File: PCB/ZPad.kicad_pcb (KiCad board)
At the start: 2 copper layers, 82 x 65.2 mm, 19 parts, among them J1 Conn_01x04, SW1 SW_Push, SW2 SW_Push, SW3 SW_Push, SW4 SW_Push, SW5 SW_Push, SW6 SW_Push, SW7 SW_Push, SW8 SW_Push, SW9 RotaryEncoder_Switch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

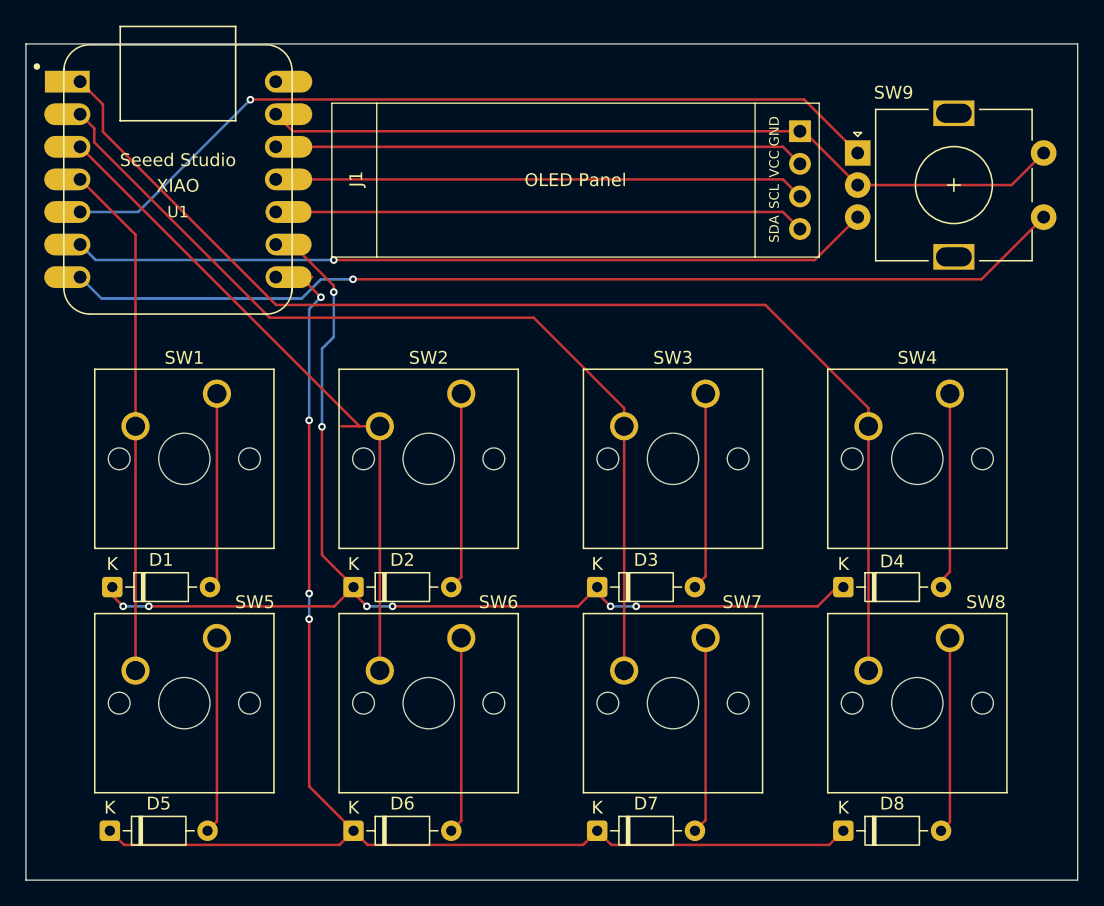
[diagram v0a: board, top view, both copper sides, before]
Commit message: Fixed stuff according to reviewer
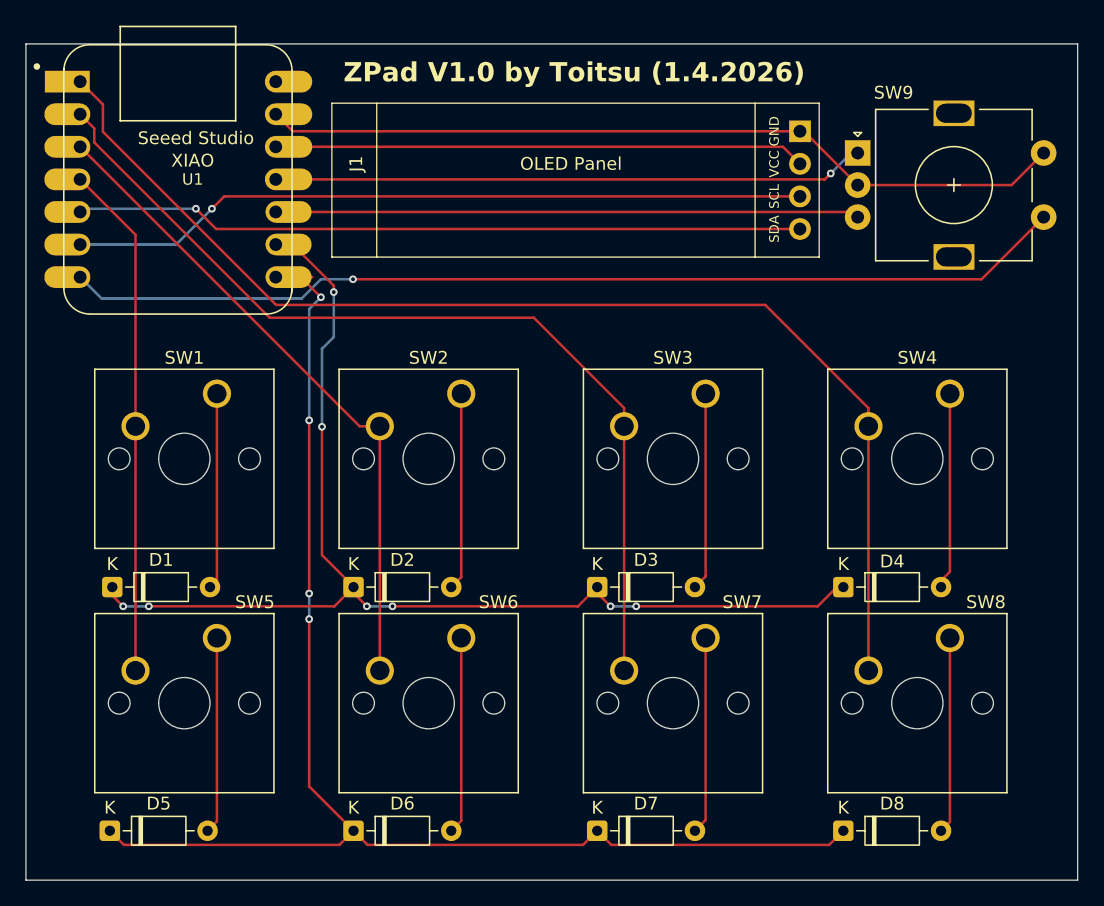
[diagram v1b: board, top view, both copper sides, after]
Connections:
- U1 pad 10: /SDA -> /Rotary_Sw_B
- U1 pad 11: /SCL -> /Rotary_Sw_A
- U1 pad 5: /Rotary_Sw_A -> /SDA
- U1 pad 6: /Rotary_Sw_B -> /SCL
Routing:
- net /Rotary_Sw_A: track 66.0 -> 47.3 mm
- net /Rotary_Sw_B: track 62.5 -> 45.5 mm, vias 1 -> 0
- net /SDA: track 41.4 -> 56.9 mm, vias 0 -> 1
- net /SCL: track 42.5 -> 57.7 mm, vias 0 -> 1
- net /COL1: track 52.9 -> 51.4 mm
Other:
- board text added: "ZPad V1.0 by Toitsu (1.4.2026)"
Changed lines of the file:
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@@
 		(at 128.35 64.27)
 		(property "Reference" "J1"
-			(at 1.9 5.91 90)
+			(at 1.9 4.73 90)
 			(layer "F.SilkS")
 			(effects
@@
 		)
 		(property "Value" "Conn_01x04"
-			(at 18.5 14 0)
+			(at 18.15 12.98 0)
 			(layer "F.Fab")
 			(effects
@@
 		)
 		(fp_text user "OLED Panel"
-			(at 19 6 0)
+			(at 18.65 4.73 0)
 			(layer "F.SilkS")
 			(effects
@@
 		)
 		(property "Value" "RotaryEncoder_Switch"
-			(at 7.5 10.4 0)
+			(at 7.5 10.845 0)
 			(layer "F.Fab")
 			(effects
@@
 		(at 116.35 70.212015)
 		(property "Reference" "U1"
-			(at 0 2.54 0)
+			(at 1.15 0 0)
 			(layer "F.SilkS")
 			(effects
@@
 		)
 		(fp_text user "Seeed Studio"
-			(at 0 -1.5 0)
+			(at 1.4 -3.212015 0)
 			(unlocked yes)
 			(layer "F.SilkS")
@@
 		)
 		(fp_text user "XIAO"
-			(at 0 0.5 0)
+			(at 1.15 -1.462015 0)
 			(unlocked yes)
 			(layer "F.SilkS")
@@
 			(layers "*.Cu" "*.Mask")
 			(remove_unused_layers no)
-			(net 21 "/Rotary_Sw_A")
+			(net 12 "/SDA")
 			(pinfunction "PA8_A4_D4_SDA")
 			(pintype "passive")
@@
 			(layers "*.Cu" "*.Mask")
 			(remove_unused_layers no)
-			(net 20 "/Rotary_Sw_B")
+			(net 13 "/SCL")
 			(pinfunction "PA9_A5_D5_SCL")
 			(pintype "passive")
@@
 			(layers "*.Cu" "*.Mask")
 			(remove_unused_layers no)
-			(net 12 "/SDA")
+			(net 20 "/Rotary_Sw_B")
 			(pinfunction "PA5_A9_D9_MISO")
 			(pintype "passive")
@@
 			(layers "*.Cu" "*.Mask")
 			(remove_unused_layers no)
-			(net 13 "/SCL")
+			(net 21 "/Rotary_Sw_A")
 			(pinfunction "PA6_A10_D10_MOSI")
 			(pintype "passive")
@@
 		(layer "Edge.Cuts")
 	)
+	(gr_text "ZPad V1.0 by Toitsu (1.4.2026)"
+		(at 129.25 62.75 0)
+		(layer "F.SilkS")
+		(effects
+			(font
+				(size 1.5 1.5)
+				(thickness 0.3)
+				(bold yes)
+			)
+			(justify left bottom)
+		)
+	)
 	(segment
 		(start 128.5 78.5)
@@
 	(segment
 		(start 164.85 74.08)
-		(end 163.522015 72.752015)
+		(end 119.33 74.08)
 		(width 0.2)
 		(layer "F.Cu")
@@
 	)
 	(segment
-		(start 163.522015 72.752015)
-		(end 123.975 72.752015)
+		(start 119.33 74.08)
+		(end 117.75 72.5)
 		(width 0.2)
 		(layer "F.Cu")
 		(net 12)
 	)
+	(via
+		(at 117.75 72.5)
+		(size 0.6)
+		(drill 0.3)
+		(layers "F.Cu" "B.Cu")
+		(net 12)
+	)
 	(segment
-		(start 163.522015 70.212015)
-		(end 123.975 70.212015)
+		(start 117.75 72.5)
+		(end 108.977015 72.5)
+		(width 0.2)
+		(layer "B.Cu")
+		(net 12)
+	)
+	(segment
+		(start 108.977015 72.5)
+		(end 108.725 72.752015)
+		(width 0.2)
+		(layer "B.Cu")
+		(net 12)
+	)
+	(segment
+		(start 164.85 71.54)
+		(end 119.96 71.54)
 		(width 0.2)
 		(layer "F.Cu")
@@
 	)
 	(segment
-		(start 164.85 71.54)
-		(end 163.522015 70.212015)
+		(start 119.96 71.54)
+		(end 119 72.5)
 		(width 0.2)
 		(layer "F.Cu")
 		(net 13)
 	)
+	(via
+		(at 119 72.5)
+		(size 0.6)
+		(drill 0.3)
+		(layers "F.Cu" "B.Cu")
+		(net 13)
+	)
 	(segment
-		(start 125.01276 70.212015)
-		(end 123.975 70.212015)
+		(start 119 72.5)
+		(end 116.207985 75.292015)
+		(width 0.2)
+		(layer "B.Cu")
+		(net 13)
+	)
+	(segment
+		(start 116.207985 75.292015)
+		(end 108.725 75.292015)
 		(width 0.2)
 		(layer "B.Cu")
@@
 	)
 	(segment
-		(start 132.09 89.46)
-		(end 129.092985 89.46)
+		(start 130.512985 89.46)
+		(end 132.09 89.46)
 		(width 0.2)
 		(layer "F.Cu")
@@
 	)
 	(segment
-		(start 166.005 76.5)
-		(end 128.5 76.5)
+		(start 168.947015 72.752015)
+		(end 169.35 73.155)
 		(width 0.2)
 		(layer "F.Cu")
@@
 	)
 	(segment
-		(start 169.35 73.155)
-		(end 166.005 76.5)
+		(start 123.975 72.752015)
+		(end 168.947015 72.752015)
 		(width 0.2)
 		(layer "F.Cu")
 		(net 20)
 	)
-	(via
-		(at 128.5 76.5)
-		(size 0.6)
-		(drill 0.3)
-		(layers "F.Cu" "B.Cu")
-		(net 20)
-	)
-	(segment
-		(start 109.932985 76.5)
-		(end 108.725 75.292015)
-		(width 0.2)
-		(layer "B.Cu")
-		(net 20)
-	)
-	(segment
-		(start 128.5 76.5)
-		(end 109.932985 76.5)
-		(width 0.2)
-		(layer "B.Cu")
-		(net 20)
-	)
 	(segment
-		(start 122.018985 63.981015)
-		(end 122 64)
+		(start 166.787985 70.212015)
+		(end 167.25 69.75)
 		(width 0.2)
 		(layer "F.Cu")
@@
 	)
 	(segment
-		(start 165.176015 63.981015)
-		(end 122.018985 63.981015)
-		(width 0.2)
-		(layer "F.Cu")
-		(net 21)
-	)
-	(segment
-		(start 169.35 68.155)
-		(end 165.176015 63.981015)
+		(start 123.975 70.212015)
+		(end 166.787985 70.212015)
 		(width 0.2)
 		(layer "F.Cu")
@@
 	)
 	(via
-		(at 122 64)
+		(at 167.25 69.75)
 		(size 0.6)
 		(drill 0.3)
@@
 	)
 	(segment
-		(start 122 64)
-		(end 113.247985 72.752015)
+		(start 168.845 68.155)
+		(end 169.35 68.155)
 		(width 0.2)
 		(layer "B.Cu")
@@
 	)
 	(segment
-		(start 113.247985 72.752015)
-		(end 108.725 72.752015)
+		(start 167.25 69.75)
+		(end 168.845 68.155)
+		(width 0.2)
+		(layer "B.Cu")
+		(net 21)
+	)
+	(segment
+		(start 125.01276 70.212015)
+		(end 123.975 70.212015)
 		(width 0.2)
 		(layer "B.Cu")
